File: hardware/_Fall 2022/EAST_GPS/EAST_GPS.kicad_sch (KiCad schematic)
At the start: 2 parts

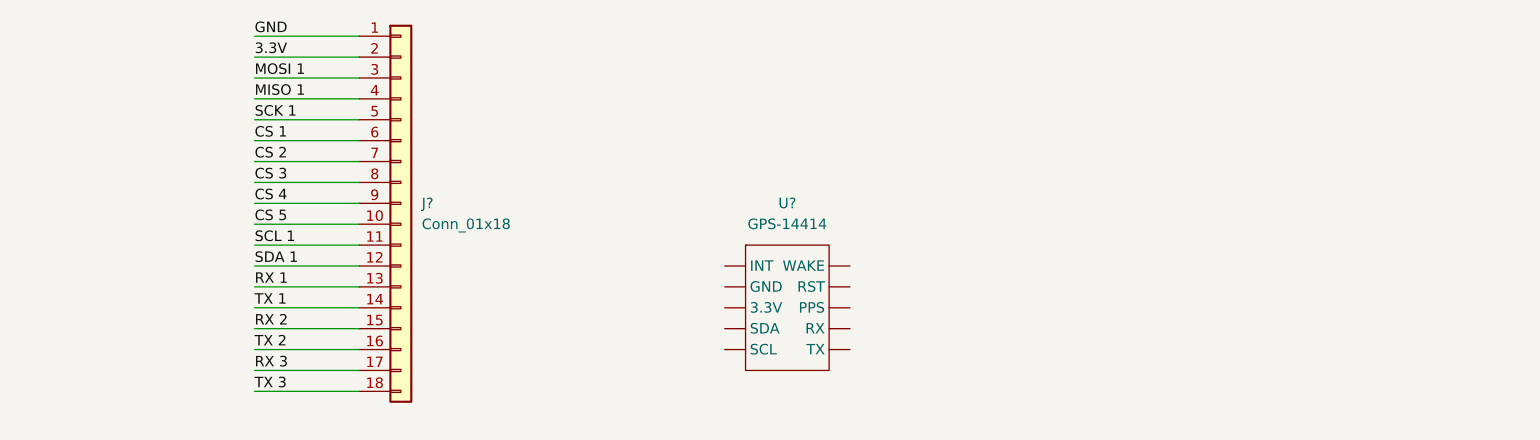
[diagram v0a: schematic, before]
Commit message: Add east teensy footprint
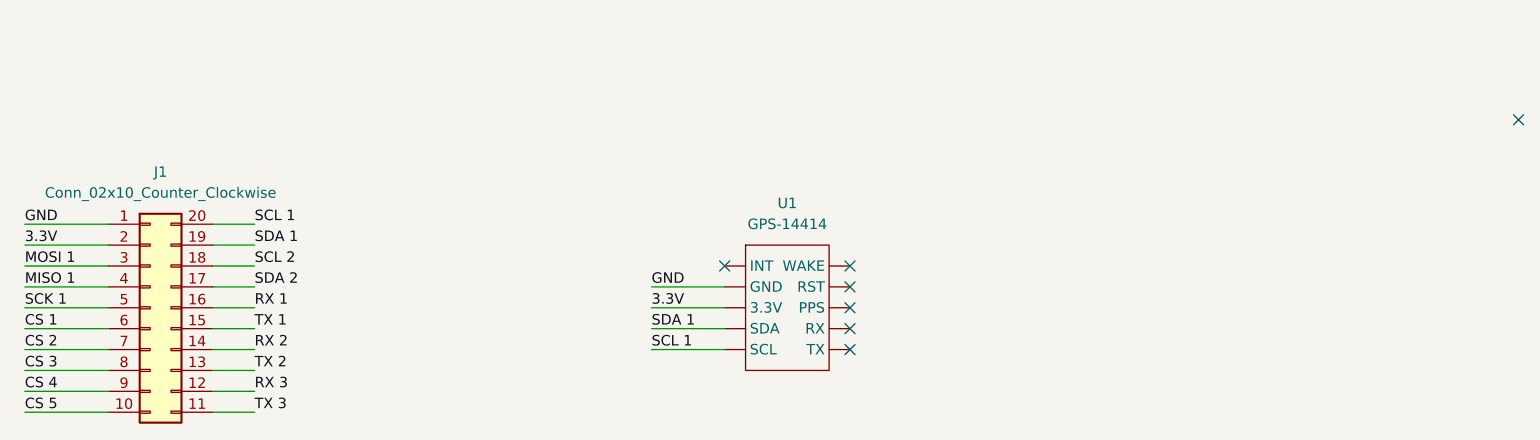
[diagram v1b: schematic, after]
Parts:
- removed J?: Conn_01x18, symbol Connector_Generic:Conn_01x18
- added J1: Conn_02x10_Counter_Clockwise, Connector_PinHeader_2.54mm:PinHeader_2x10_P2.54mm_Vertical, symbol Connector_Generic:Conn_02x10_Counter_Clockwise
- U1: renamed from U?; footprint (none) -> GPS_layout:GPS-14414
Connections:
- net 3.3V: now also U1. (WAKE), J1.2 (Pin_2)
- net CS 1: now also J1.6 (Pin_6)
- net CS 2: now also J1.7 (Pin_7)
- net CS 3: now also J1.8 (Pin_8)
- net CS 4: now also J1.9 (Pin_9)
- net CS 5: now also J1.10 (Pin_10)
- net GND: now also U1. (WAKE), J1.1 (Pin_1)
- net MISO 1: now also J1.4 (Pin_4)
- net MOSI 1: now also J1.3 (Pin_3)
- net RX 1: now also J1.16 (Pin_16)
- net RX 2: now also J1.14 (Pin_14)
- net RX 3: now also J1.12 (Pin_12)
- net SCK 1: now also J1.5 (Pin_5)
- net SCL 1: now also U1. (WAKE), J1.20 (Pin_20)
- net SDA 1: now also U1. (WAKE), J1.19 (Pin_19)
- net TX 1: now also J1.15 (Pin_15)
- net TX 2: now also J1.13 (Pin_13)
- net TX 3: now also J1.11 (Pin_11)
- new net SCL 2: J1.18 (Pin_18)
- new net SDA 2: J1.17 (Pin_17)
- no-connect marks 0 -> 7

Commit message: Update east communication and layout
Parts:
- removed J1: Conn_02x10_Counter_Clockwise, Connector_PinHeader_2.54mm:PinHeader_2x10_P2.54mm_Vertical, symbol Connector_Generic:Conn_02x10_Counter_Clockwise
- added J1: Conn_02x08_Counter_Clockwise, Connector_PinHeader_2.54mm:PinHeader_2x08_P2.54mm_Vertical, symbol Connector_Generic:Conn_02x08_Counter_Clockwise
- added J?: Conn_02x08_Odd_Even, Connector_PinHeader_2.54mm:PinHeader_2x08_P2.54mm_Vertical, symbol Connector_Generic:Conn_02x08_Odd_Even
- added U2: RFM69HCW_Breakout, Sensors:RFM69HCW_Breakout, symbol sensors:RFM69HCW_Breakout
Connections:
- net 3.3V: now also J1.2 (Pin_2), J?.9 (Pin_9), U2.1 (VIN)
- net CS 1: now also J1.6 (Pin_6), J?.4 (Pin_4), U2.8 (CS)
- net CS 2: now also J1.7 (Pin_7), J?.6 (Pin_6)
- net CS 3: now also J1.8 (Pin_8), J?.15 (Pin_15)
- net GND: now also J1.1 (Pin_1), J?.2 (Pin_2), U2.2 (GND)
- net MISO 1: now also J1.4 (Pin_4), J?.10 (Pin_10), U2.7 (MOSI)
- net MOSI 1: now also J1.3 (Pin_3), J?.8 (Pin_8), U2.6 (MISO)
- net RX 1: now also J1.12 (Pin_12), J?.13 (Pin_13)
- net RX 2: now also J1.10 (Pin_10), J?.1 (Pin_1)
- net SCK 1: now also J1.5 (Pin_5), J?.16 (Pin_16), U2.5 (SCK)
- net SCL 1: now also J1.16 (Pin_16), J?.5 (Pin_5)
- net SCL 2: now also J1.14 (Pin_14), J?.12 (Pin_12)
- net SDA 1: now also J1.15 (Pin_15), J?.7 (Pin_7)
- net SDA 2: now also J1.13 (Pin_13), J?.14 (Pin_14)
- net TX 1: now also J1.11 (Pin_11), J?.11 (Pin_11)
- net TX 2: now also J1.9 (Pin_9), J?.3 (Pin_3)
- no-connect marks 7 -> 15
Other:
- note added: "EAST Communication"
- note added: "GPS"
- note added: "Radio"
- moved on the sheet: U1

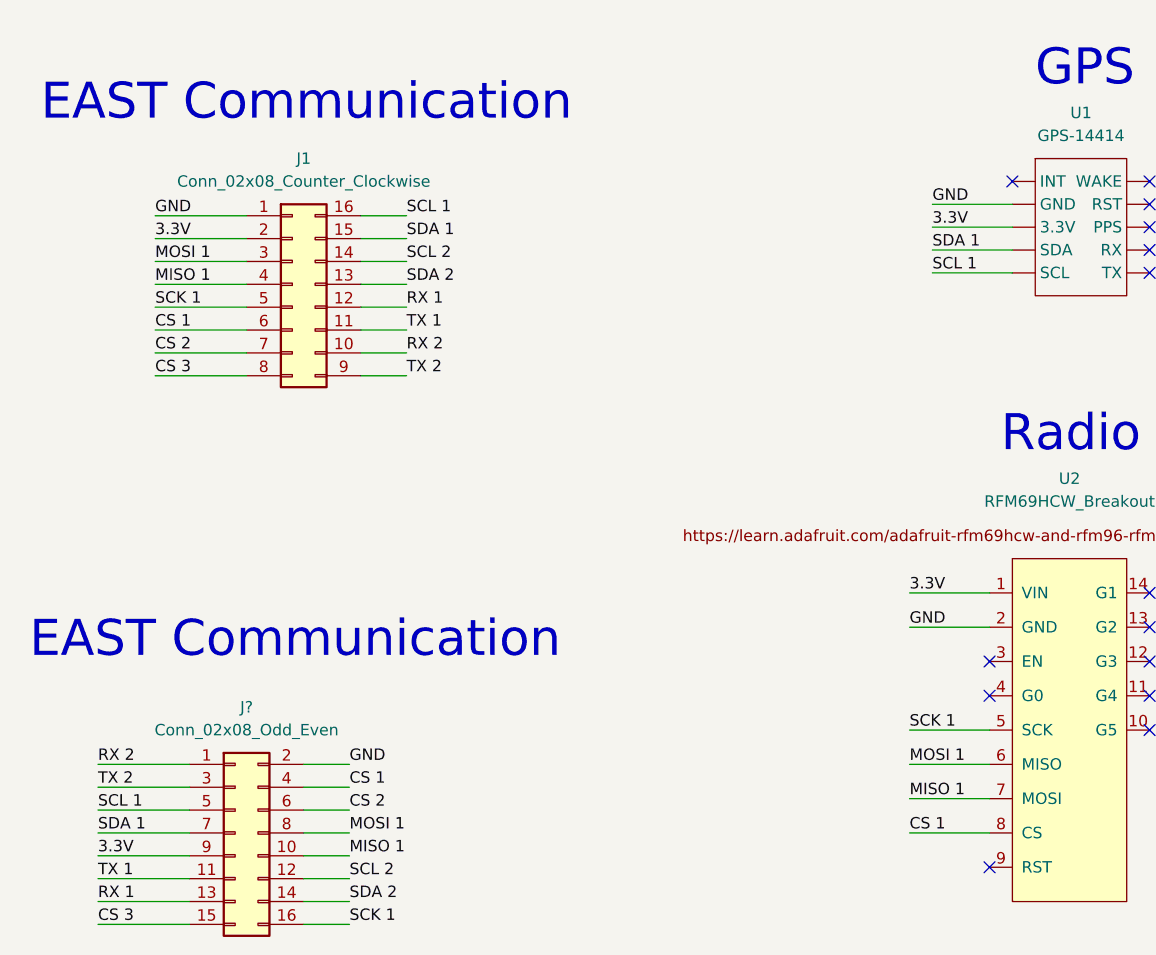
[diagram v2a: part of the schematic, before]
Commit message: Update pin connections
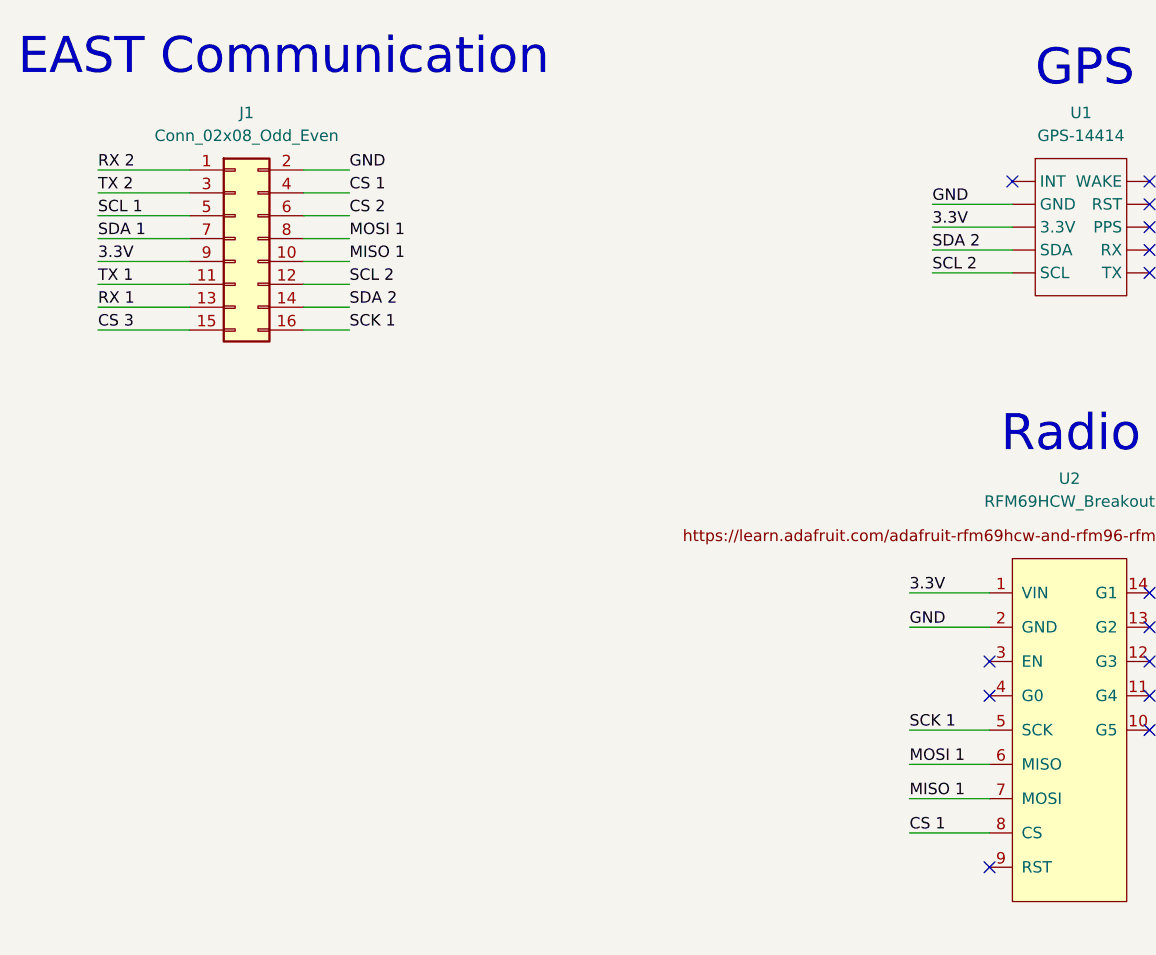
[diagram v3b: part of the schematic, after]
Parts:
- removed J1: Conn_02x08_Counter_Clockwise, Connector_PinHeader_2.54mm:PinHeader_2x08_P2.54mm_Vertical, symbol Connector_Generic:Conn_02x08_Counter_Clockwise
- removed J?: Conn_02x08_Odd_Even, Connector_PinHeader_2.54mm:PinHeader_2x08_P2.54mm_Vertical, symbol Connector_Generic:Conn_02x08_Odd_Even
- added J1: Conn_02x08_Odd_Even, Connector_PinHeader_2.54mm:PinHeader_2x08_P2.54mm_Vertical, symbol Connector_Generic:Conn_02x08_Odd_Even
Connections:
- net 3.3V: now also J1.9 (Pin_9)
- net CS 1: now also J1.4 (Pin_4)
- net CS 2: now also J1.6 (Pin_6)
- net CS 3: now also J1.15 (Pin_15)
- net GND: now also J1.2 (Pin_2)
- net MISO 1: now also J1.10 (Pin_10)
- net MOSI 1: now also J1.8 (Pin_8)
- net RX 1: now also J1.13 (Pin_13)
- net RX 2: now also J1.1 (Pin_1)
- net SCK 1: now also J1.16 (Pin_16)
- net SCL 1: now also J1.5 (Pin_5); no longer U1. (WAKE)
- net SCL 2: now also U1. (WAKE), J1.12 (Pin_12)
- net SDA 1: now also J1.7 (Pin_7); no longer U1. (WAKE)
- net SDA 2: now also U1. (WAKE), J1.14 (Pin_14)
- net TX 1: now also J1.11 (Pin_11)
- net TX 2: now also J1.3 (Pin_3)

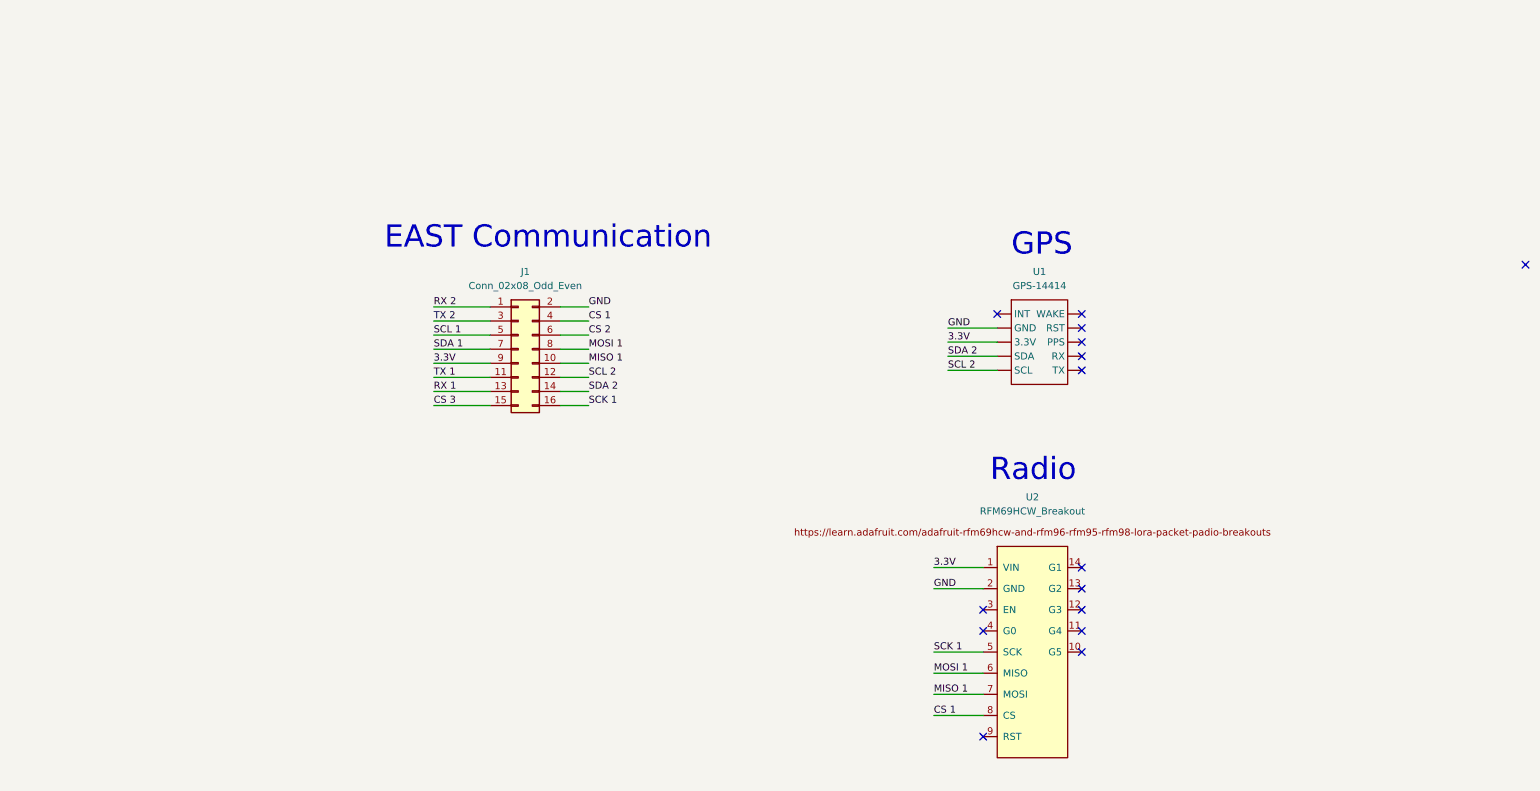
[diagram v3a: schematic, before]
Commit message: reorganize shematic
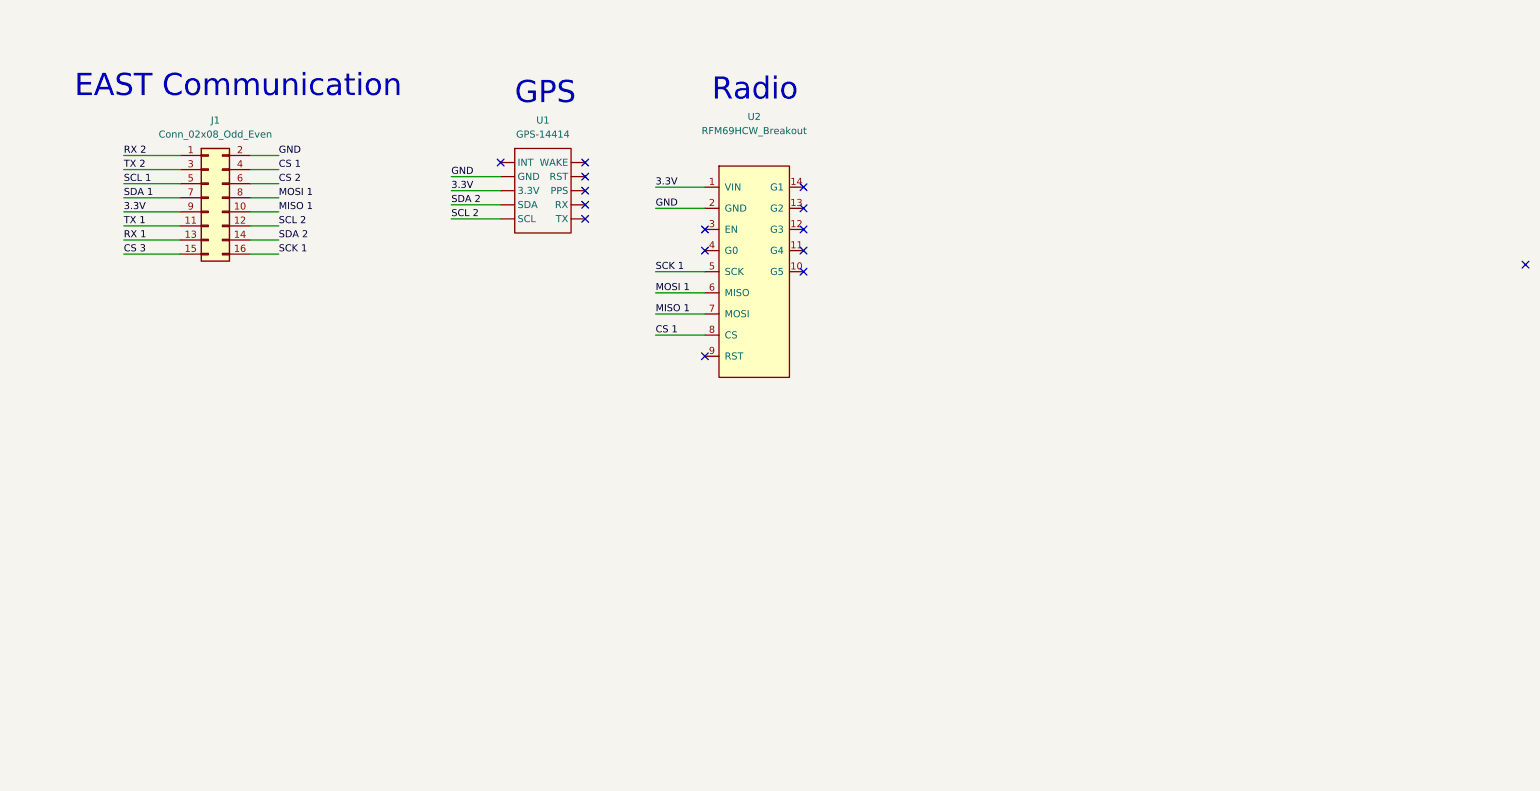
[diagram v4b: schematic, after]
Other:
- moved on the sheet: J1, U1
